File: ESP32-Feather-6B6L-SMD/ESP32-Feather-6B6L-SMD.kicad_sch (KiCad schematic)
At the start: 1 part

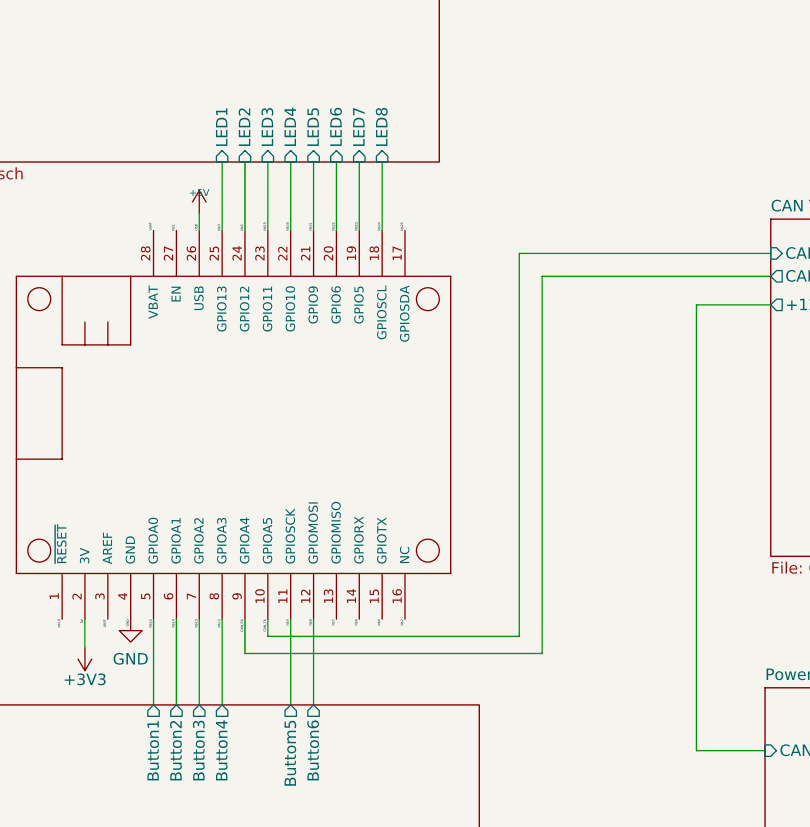
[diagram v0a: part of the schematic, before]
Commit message: Rescue SCL.
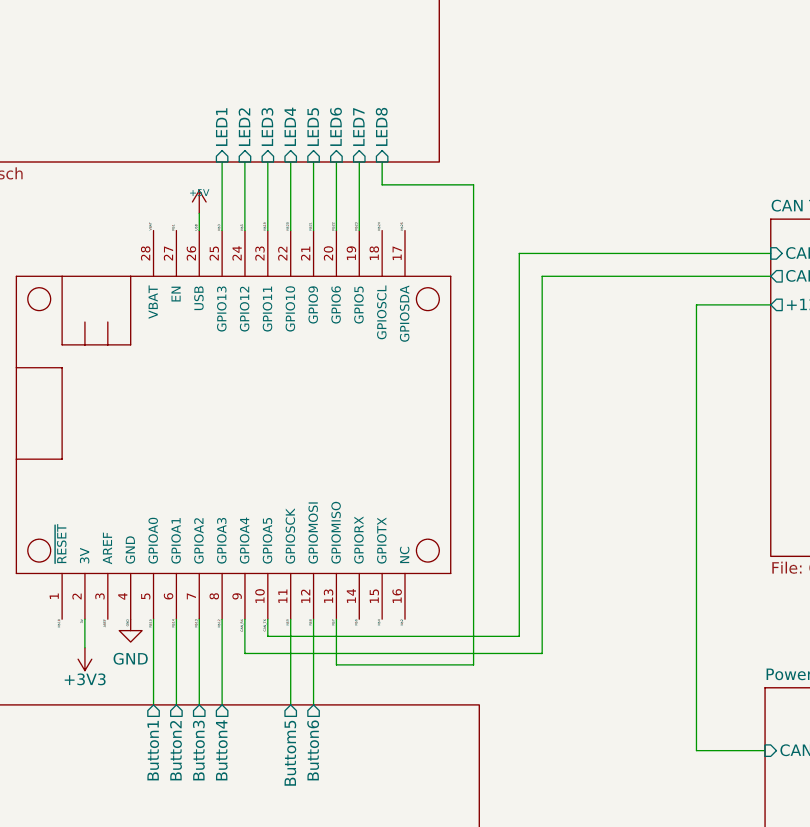
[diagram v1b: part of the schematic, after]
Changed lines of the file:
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@@
     (stroke (width 0) (type default) (color 0 0 0 0))
   )
-  (wire (pts (xy 125.095 59.055) (xy 125.095 66.675))
+  (wire (pts (xy 135.255 61.595) (xy 135.255 114.935))
     (stroke (width 0) (type default) (color 0 0 0 0))
   )
@@
     (stroke (width 0) (type default) (color 0 0 0 0))
   )
+  (wire (pts (xy 125.095 59.055) (xy 125.095 61.595))
+    (stroke (width 0) (type default) (color 0 0 0 0))
+  )
   (wire (pts (xy 117.475 59.055) (xy 117.475 66.675))
     (stroke (width 0) (type default) (color 0 0 0 0))
   )
   (wire (pts (xy 92.075 109.855) (xy 92.075 113.03))
+    (stroke (width 0) (type default) (color 0 0 0 0))
+  )
+  (wire (pts (xy 135.255 114.935) (xy 120.015 114.935))
     (stroke (width 0) (type default) (color 0 0 0 0))
   )
@@
     (stroke (width 0) (type default) (color 0 0 0 0))
   )
+  (wire (pts (xy 125.095 61.595) (xy 135.255 61.595))
+    (stroke (width 0) (type default) (color 0 0 0 0))
+  )
   (wire (pts (xy 160.02 124.46) (xy 167.64 124.46))
     (stroke (width 0) (type default) (color 0 0 0 0))
@@
     (stroke (width 0) (type default) (color 0 0 0 0))
   )
+  (wire (pts (xy 120.015 114.935) (xy 120.015 109.855))
+    (stroke (width 0) (type default) (color 0 0 0 0))
+  )
